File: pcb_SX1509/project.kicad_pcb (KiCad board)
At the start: 2 copper layers, 18.3 x 25.9 mm, 43 parts, among them IC1 SX1509QBIULTRT

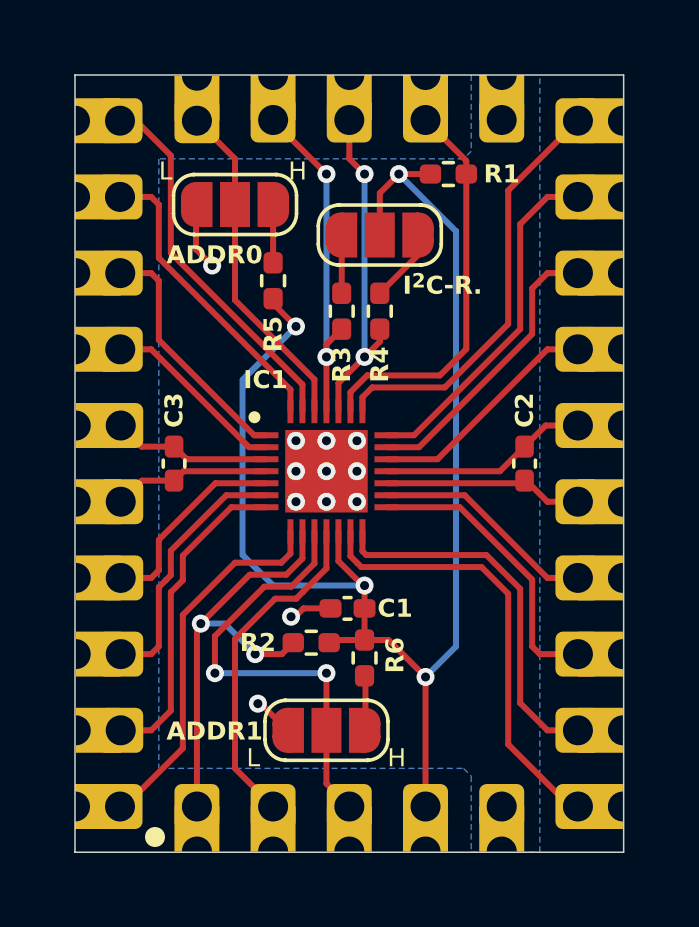
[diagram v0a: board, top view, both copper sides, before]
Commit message: Standard output pin design for SX1509 PCB and add a new variant based on PCA9685
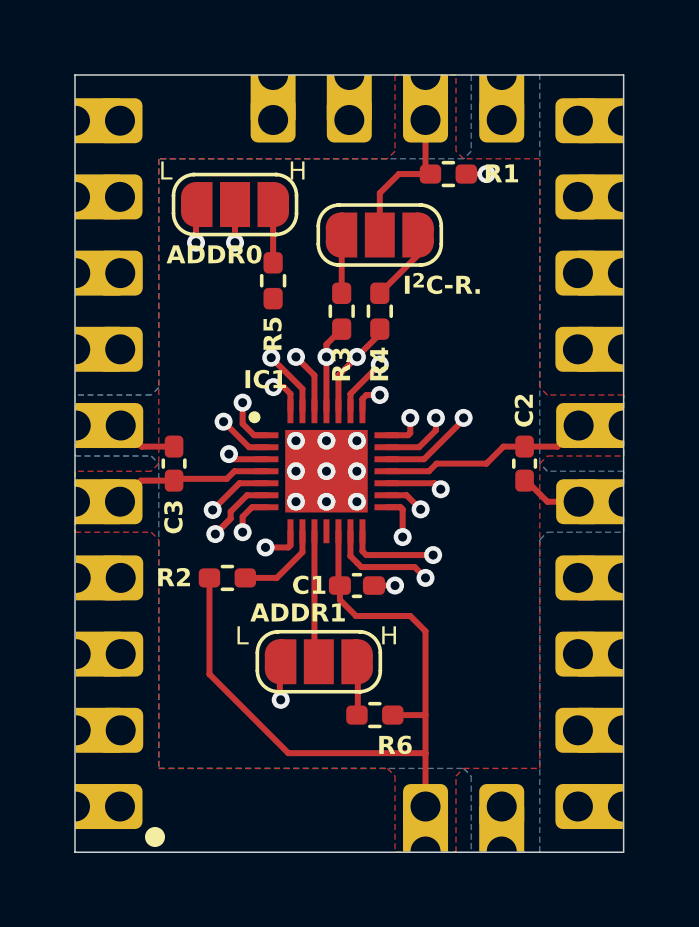
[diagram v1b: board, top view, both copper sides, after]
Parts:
- removed J24, J25, J26, J27: ~, Castellated_Holes:Castellated_Hole02
- moved J17 18.4 mm to (114.8, 89.9), turned to 180 degrees
- moved J19 18.4 mm to (96.5, 92.5), turned to 0 degrees
- moved J23 7.62 mm to (108.2, 78.2)
- moved R2 3.53 mm to (101.6, 95.0), turned to 180 degrees
- moved JP3 2.30 mm to (104.6, 97.8)
- moved R6 1.94 mm to (106.5, 99.6), turned to 0 degrees
- moved C1 0.82 mm to (105.9, 95.2), turned to 0 degrees
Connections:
- C2 pad 1: /VCC2 -> +3.3V
- C2 pad 2: /GNDD2 -> GNDD
- C3 pad 1: /VCC1 -> +3.3V
- C3 pad 2: /GNDD1 -> GNDD
- IC1 pad 11: /OSCIO -> unconnected-(IC1-OSCIO-Pad11)
- IC1 pad 17: /GNDD2 -> GNDD
- IC1 pad 18: /VCC2 -> +3.3V
- IC1 pad 3: /GNDD1 -> GNDD
- IC1 pad 4: /VCC1 -> +3.3V
- J17 pad 1: /VCC1 -> +3.3V
- J18 pad 1: /GNDD1 -> GNDD
- J19 pad 1: /VCC2 -> +3.3V
- J20 pad 1: /GNDD2 -> GNDD
- J23 pad 1: /ADDR0 -> +3.3V
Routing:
- net /~{INT}: track 15.0 -> 2.96 mm, vias 2 -> 0
- net /OSCIO: track 11.4 -> 0.00 mm
- net /ADDR1: track 15.2 -> 4.41 mm, vias 2 -> 0
- net /VCC2: track 7.01 -> 0.00 mm
- net /GNDD2: track 6.84 -> 0.00 mm
- net GNDD: track 5.04 -> 10.9 mm, vias 12 -> 14
- net +3.3V: track 47.5 -> 41.8 mm, vias 4 -> 0
- net /GNDD1: track 5.32 -> 0.00 mm
- net /VCC1: track 5.28 -> 0.00 mm
- net /ADDR0: track 11.3 -> 7.99 mm, vias 0 -> 2
- net /~{RESET}: track 13.3 -> 10.5 mm, vias 0 -> 2
- net /IO15: track 14.1 -> 13.1 mm, vias 0 -> 1
- net /IO10: track 9.72 -> 10.3 mm, vias 0 -> 1
- net /IO4: track 8.78 -> 8.31 mm, vias 0 -> 1
- net /IO13: track 9.68 -> 10.1 mm, vias 0 -> 1
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- added copper zone on F.Cu, net +3.3V
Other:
- copper layers 2 -> 4
- board text removed: "OSCIO"
- board text removed: "VCC1"
- board text removed: "VCC2"
- board text removed: "~{INT}"
- board text removed: "~{RESET}"

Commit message: Update PCB for PCA9685
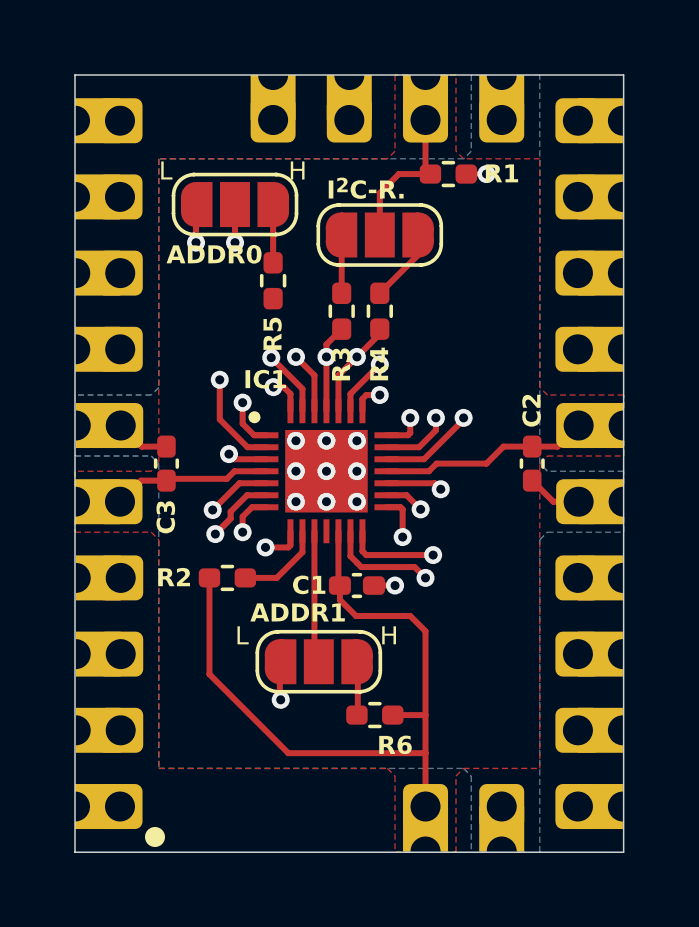
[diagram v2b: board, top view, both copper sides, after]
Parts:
- moved C2 0.25 mm to (111.8, 91.2)
- moved C3 0.25 mm to (99.6, 91.2)
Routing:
- net /IO3: track 8.25 -> 9.02 mm
- net GNDD: track 10.9 -> 10.2 mm
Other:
- board text removed: "GND1"
- board text removed: "GND2"
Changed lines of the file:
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@@
 		(tags "resistor handsolder")
 		(property "Reference" "R6"
-			(at 0.6725 1.016 360)
+			(at 0.6725 1.016 0)
 			(layer "F.SilkS")
 			(effects
@@
 		)
 		(property "Value" "10k"
-			(at 0 1.17 360)
+			(at 0 1.17 0)
 			(layer "F.Fab")
 			(hide yes)
@@
 		)
 		(fp_text user "${REFERENCE}"
-			(at 0 0 360)
+			(at 0 0 0)
 			(layer "F.Fab")
 			(effects
@@
 	(footprint "Capacitor_SMD:C_0402_1005Metric_Pad0.74x0.62mm_HandSolder"
 		(layer "F.Cu")
-		(at 99.822 91.186 90)
+		(at 99.568 91.186 90)
 		(descr "Capacitor SMD 0402 (1005 Metric), square (rectangular) end terminal, IPC_7351 nominal with elongated pad for handsoldering. (Body size source: IPC-SM-782 page 76, https://www.pcb-3d.com/wordpress/wp-content/uploads/ipc-sm-782a_amendment_1_and_2.pdf), generated with kicad-footprint-generator")
 		(tags "capacitor handsolder")
@@
 	(footprint "Capacitor_SMD:C_0402_1005Metric_Pad0.74x0.62mm_HandSolder"
 		(layer "F.Cu")
-		(at 111.506 91.186 -90)
+		(at 111.76 91.186 -90)
 		(descr "Capacitor SMD 0402 (1005 Metric), square (rectangular) end terminal, IPC_7351 nominal with elongated pad for handsoldering. (Body size source: IPC-SM-782 page 76, https://www.pcb-3d.com/wordpress/wp-content/uploads/ipc-sm-782a_amendment_1_and_2.pdf), generated with kicad-footprint-generator")
 		(tags "capacitor handsolder")
@@
 		(tags "capacitor handsolder")
 		(property "Reference" "C1"
-			(at -1.5835 0 360)
+			(at -1.5835 0 0)
 			(layer "F.SilkS")
 			(effects
@@
 		)
 		(property "Value" "0.1uF"
-			(at 0 1.16 360)
+			(at 0 1.16 0)
 			(layer "F.Fab")
 			(hide yes)
@@
 		)
 		(fp_text user "${REFERENCE}"
-			(at 0 0 360)
+			(at 0 0 0)
 			(layer "F.Fab")
 			(effects
@@
 		)
 	)
-	(gr_text "GND1"
+	(gr_text "GND"
 		(at 99.06 89.154 0)
 		(layer "B.SilkS")
@@
 		)
 	)
-	(gr_text "GND2"
+	(gr_text "GND"
 		(at 114.3 91.694 0)
 		(layer "B.SilkS")
@@
 	)
 	(gr_text "I^{2}C-R."
-		(at 107.442 85.598 0)
+		(at 104.902 82.423 0)
 		(layer "F.SilkS")
 		(effects
@@
 	)
 	(segment
-		(start 112.268 92.456)
-		(end 113.284 92.456)
-		(width 0.2)
-		(layer "F.Cu")
-		(net 9)
-	)
-	(segment
 		(start 108.512 91.84)
 		(end 106.902 91.84)
@@
 	)
 	(segment
-		(start 101.823902 91.04)
-		(end 102.902 91.04)
+		(start 98.7465 90.6185)
+		(end 98.044 89.916)
 		(width 0.2)
 		(layer "F.Cu")
@@
 	)
 	(segment
-		(start 111.506 91.7535)
-		(end 111.5655 91.7535)
+		(start 99.568 90.6185)
+		(end 98.7465 90.6185)
 		(width 0.2)
 		(layer "F.Cu")
@@
 	)
 	(segment
-		(start 111.4195 91.84)
-		(end 111.506 91.7535)
+		(start 101.823902 91.04)
+		(end 102.902 91.04)
 		(width 0.2)
 		(layer "F.Cu")
@@
 	)
 	(segment
-		(start 98.7465 90.6185)
-		(end 98.044 89.916)
+		(start 111.76 91.7535)
+		(end 112.4625 92.456)
 		(width 0.2)
 		(layer "F.Cu")
@@
 	)
 	(segment
-		(start 99.822 90.6185)
-		(end 98.7465 90.6185)
+		(start 112.4625 92.456)
+		(end 113.284 92.456)
 		(width 0.2)
 		(layer "F.Cu")
@@
 	)
 	(segment
-		(start 111.5655 91.7535)
-		(end 112.268 92.456)
-		(width 0.2)
-		(layer "F.Cu")
-		(net 9)
-	)
-	(segment
-		(start 113.1925 92.5475)
-		(end 113.284 92.456)
+		(start 113.284 92.456)
+		(end 113.1925 92.5475)
 		(width 0.2)
 		(layer "F.Cu")
@@
 	)
 	(segment
-		(start 99.8815 91.694)
-		(end 99.822 91.7535)
+		(start 110.236 91.186)
+		(end 110.8035 90.6185)
 		(width 0.2)
 		(layer "F.Cu")
@@
 	)
 	(segment
-		(start 111.506 90.6185)
-		(end 112.6055 90.6185)
+		(start 112.6055 90.6185)
+		(end 113.308 89.916)
 		(width 0.2)
 		(layer "F.Cu")
@@
 	)
 	(segment
-		(start 101.836968 91.44)
-		(end 101.582968 91.694)
-		(width 0.2)
-		(layer "F.Cu")
-		(net 17)
-	)
-	(segment
 		(start 107.696 96.266)
 		(end 108.204 96.774)
@@
 	)
 	(segment
-		(start 108.319372 91.44)
-		(end 108.573372 91.186)
+		(start 99.568 91.7535)
+		(end 98.7225 91.7535)
 		(width 0.2)
 		(layer "F.Cu")
@@
 	)
 	(segment
-		(start 98.7225 91.7535)
-		(end 98.02 92.456)
+		(start 101.836968 91.44)
+		(end 101.582968 91.694)
+		(width 0.2)
+		(layer "F.Cu")
+		(net 17)
+	)
+	(segment
+		(start 106.902 91.44)
+		(end 108.319372 91.44)
 		(width 0.2)
 		(layer "F.Cu")
@@
 	)
 	(segment
-		(start 106.902 91.44)
-		(end 108.319372 91.44)
-		(width 0.2)
-		(layer "F.Cu")
-		(net 17)
-	)
-	(segment
-		(start 103.124 85.852)
-		(end 103.124 85.6875)
+		(start 101.582968 91.694)
+		(end 99.6275 91.694)
 		(width 0.2)
 		(layer "F.Cu")
@@
 	)
 	(segment
-		(start 108.204 79.732)
-		(end 108.204 81.3695)
+		(start 108.319372 91.44)
+		(end 108.573372 91.186)
 		(width 0.2)
 		(layer "F.Cu")
@@
 	)
 	(segment
-		(start 108.204 81.3695)
-		(end 108.3685 81.534)
+		(start 103.124 85.852)
+		(end 103.124 85.6875)
 		(width 0.2)
 		(layer "F.Cu")
@@
 	)
 	(segment
-		(start 107.315 81.534)
-		(end 106.68 82.169)
+		(start 108.204 79.732)
+		(end 108.204 81.3695)
 		(width 0.2)
 		(layer "F.Cu")
@@
 	)
 	(segment
-		(start 112.6055 90.6185)
-		(end 113.308 89.916)
+		(start 108.204 81.3695)
+		(end 108.3685 81.534)
 		(width 0.2)
 		(layer "F.Cu")
@@
 	)
 	(segment
-		(start 110.236 91.186)
-		(end 110.8035 90.6185)
+		(start 107.315 81.534)
+		(end 106.68 82.169)
 		(width 0.2)
 		(layer "F.Cu")
@@
 	(segment
 		(start 110.8035 90.6185)
-		(end 111.506 90.6185)
+		(end 112.6055 90.6185)
 		(width 0.2)
 		(layer "F.Cu")
@@
 	)
 	(segment
-		(start 99.822 91.7535)
-		(end 98.7225 91.7535)
+		(start 98.7225 91.7535)
+		(end 98.02 92.456)
 		(width 0.2)
 		(layer "F.Cu")
@@
 	)
 	(segment
-		(start 101.582968 91.694)
-		(end 99.8815 91.694)
+		(start 99.6275 91.694)
+		(end 99.568 91.7535)
 		(width 0.2)
 		(layer "F.Cu")
@@
 	)
 	(segment
-		(start 101.473 89.789)
-		(end 102.324 90.64)
+		(start 102.272431 90.64)
+		(end 101.346 89.713569)
 		(width 0.2)
 		(layer "F.Cu")
@@
 	)
 	(segment
-		(start 96.528 87.376)
-		(end 98.552 87.376)
+		(start 101.346 89.713569)
+		(end 101.346 88.392)
+		(width 0.2)
+		(layer "F.Cu")
+		(net 19)
+	)
+	(segment
+		(start 102.902 90.64)
+		(end 102.272431 90.64)
 		(width 0.2)
 		(layer "F.Cu")
@@
 	)
 	(segment
-		(start 102.324 90.64)
-		(end 102.902 90.64)
+		(start 96.528 87.376)
+		(end 98.552 87.376)
 		(width 0.2)
 		(layer "F.Cu")
@@
 	)
 	(via blind
-		(at 101.473 89.789)
+		(at 101.346 88.392)
 		(size 0.6)
 		(drill 0.3)
@@
 	)
 	(segment
-		(start 99.06 87.376)
-		(end 98.028 87.376)
+		(start 101.346 88.392)
+		(end 100.33 87.376)
 		(width 0.2)
 		(layer "In2.Cu")
@@
 	)
 	(segment
-		(start 101.473 89.789)
-		(end 99.06 87.376)
+		(start 100.33 87.376)
+		(end 98.028 87.376)
 		(width 0.2)
 		(layer "In2.Cu")

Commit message: Add barcode with the GitHub repository URL on the backsite of the PCBs
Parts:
- added G***: LOGO, LOGO, B.Cu at (107.1, 86.9)

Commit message: Replace QRCode with better version
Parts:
- removed G***: LOGO, LOGO
- added QR*****: https://github.com/fanningert/kicad_pcb_ioexpander, https://github.com/fanningert/kicad_pcb_ioexpander, B.Cu at (105.6, 87.7)

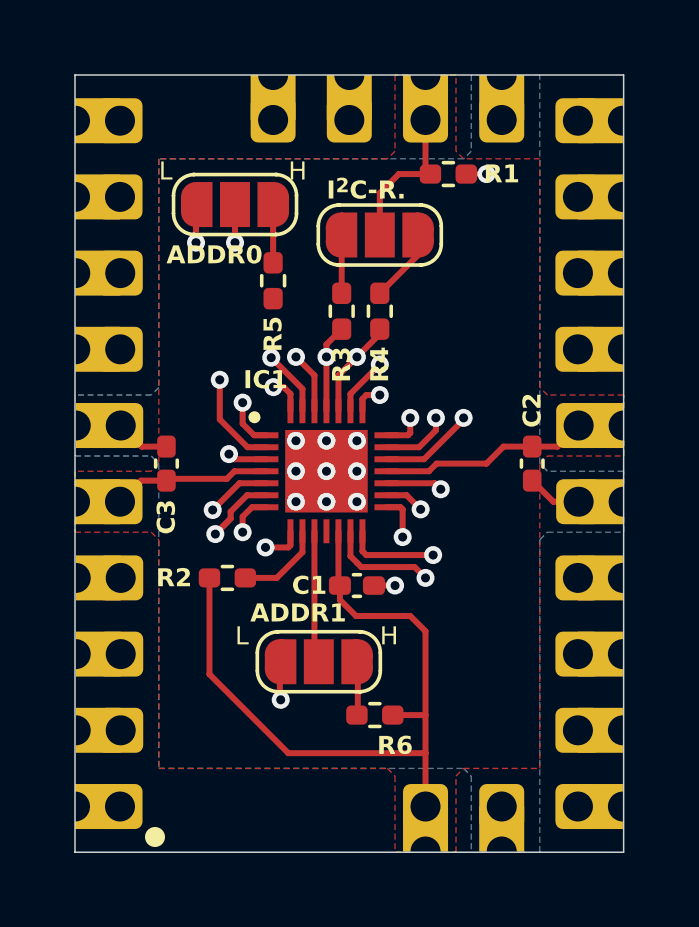
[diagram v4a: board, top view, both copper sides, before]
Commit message: Remove connector on own side
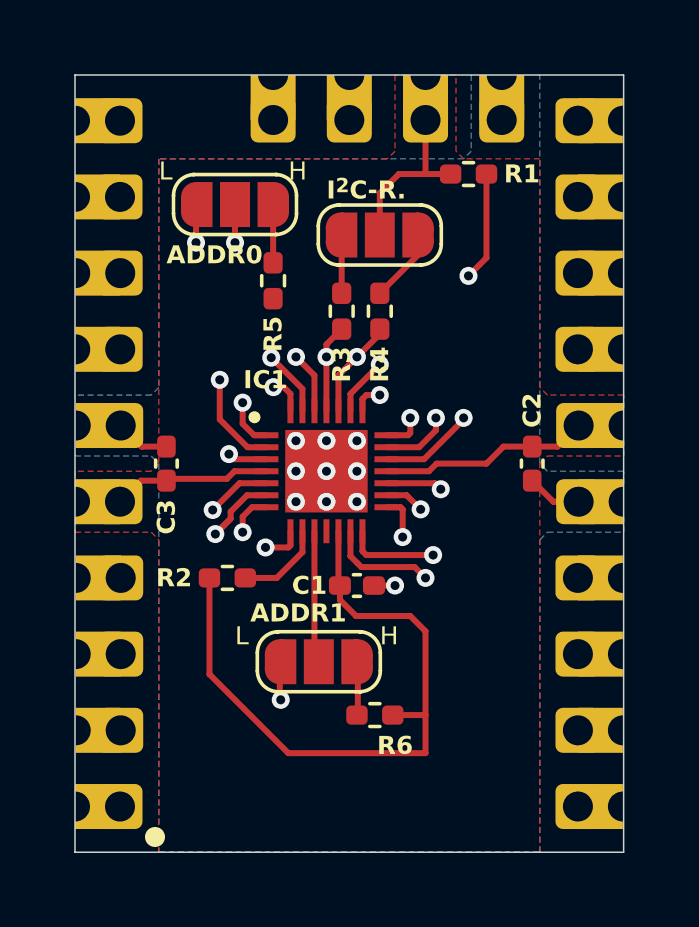
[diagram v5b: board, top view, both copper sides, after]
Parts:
- removed J21, J22: ~, Castellated_Holes:Castellated_Hole02
- moved R1 0.67 mm to (109.6, 81.5)
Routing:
- net +3.3V: track 41.8 -> 40.6 mm
- net /~{RESET}: track 10.5 -> 9.78 mm
